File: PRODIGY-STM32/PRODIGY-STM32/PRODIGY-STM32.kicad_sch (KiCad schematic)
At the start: 4 parts

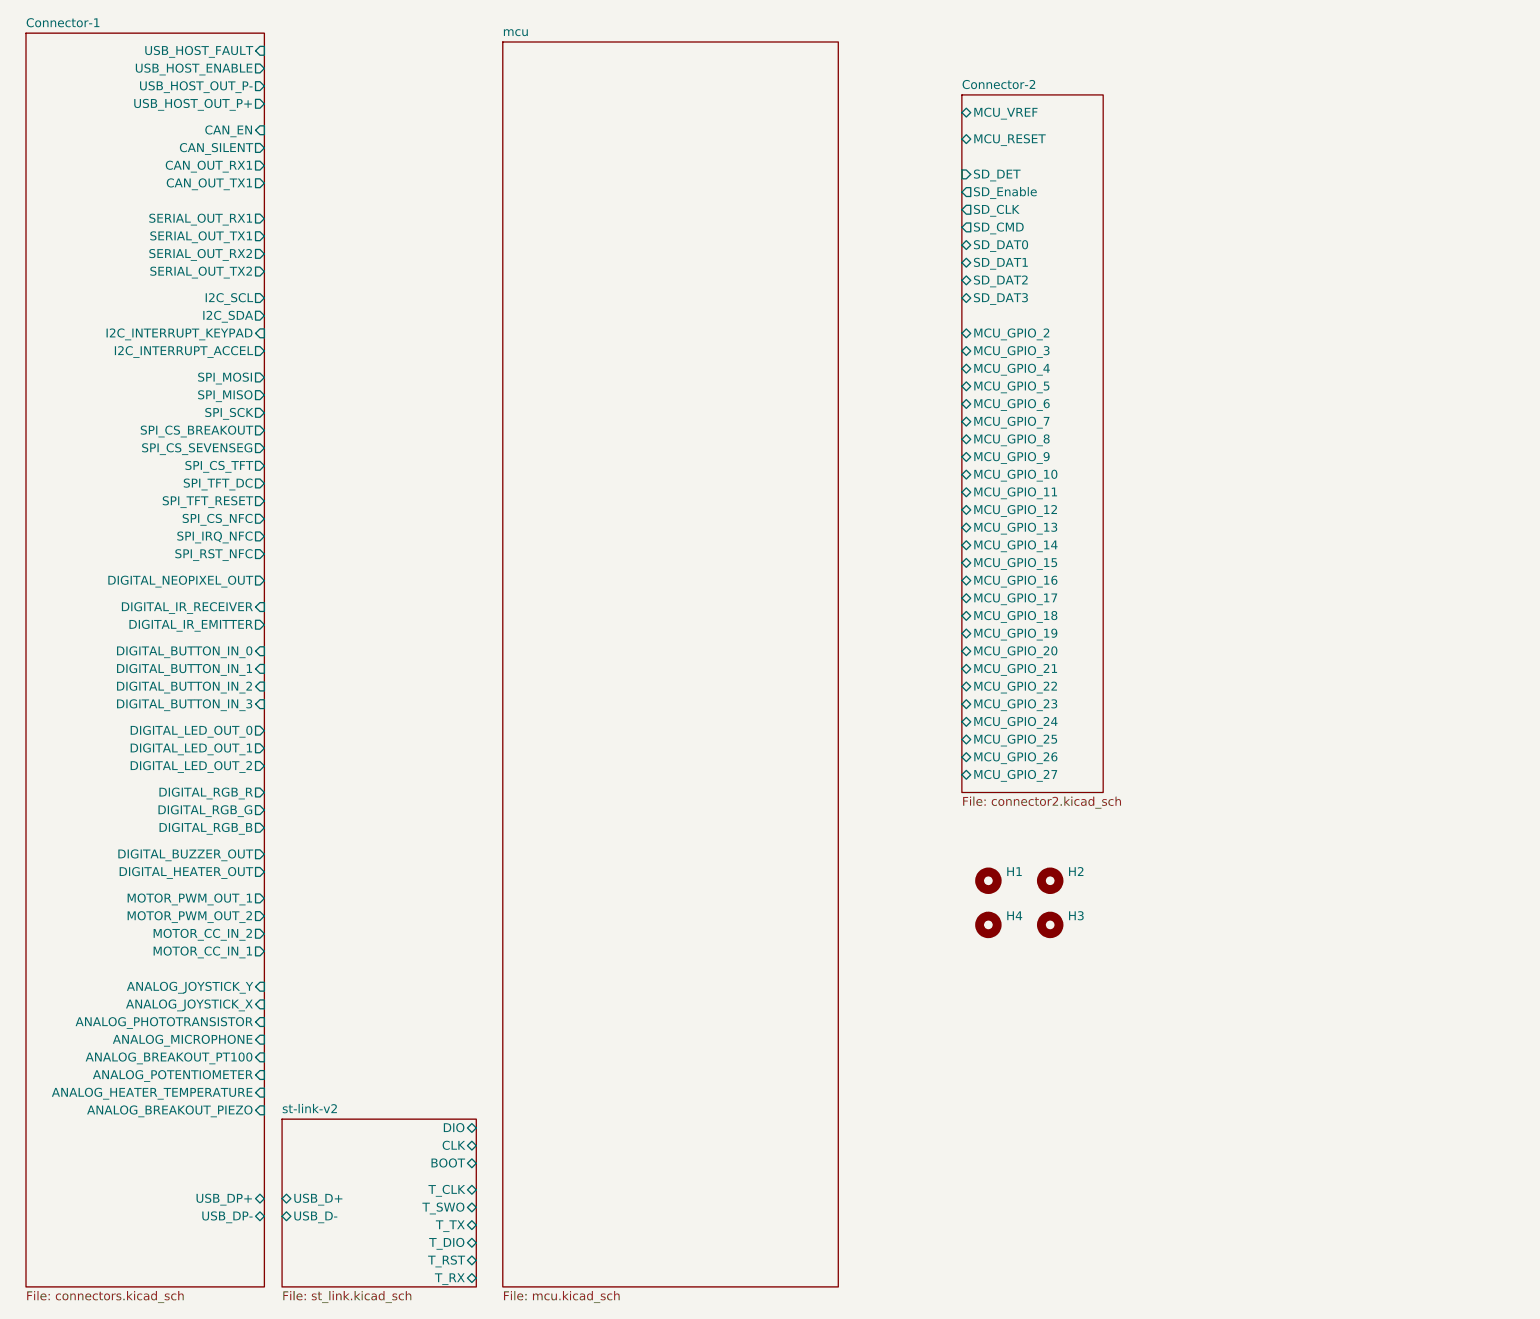
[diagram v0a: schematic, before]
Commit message: stm32 schematic finished
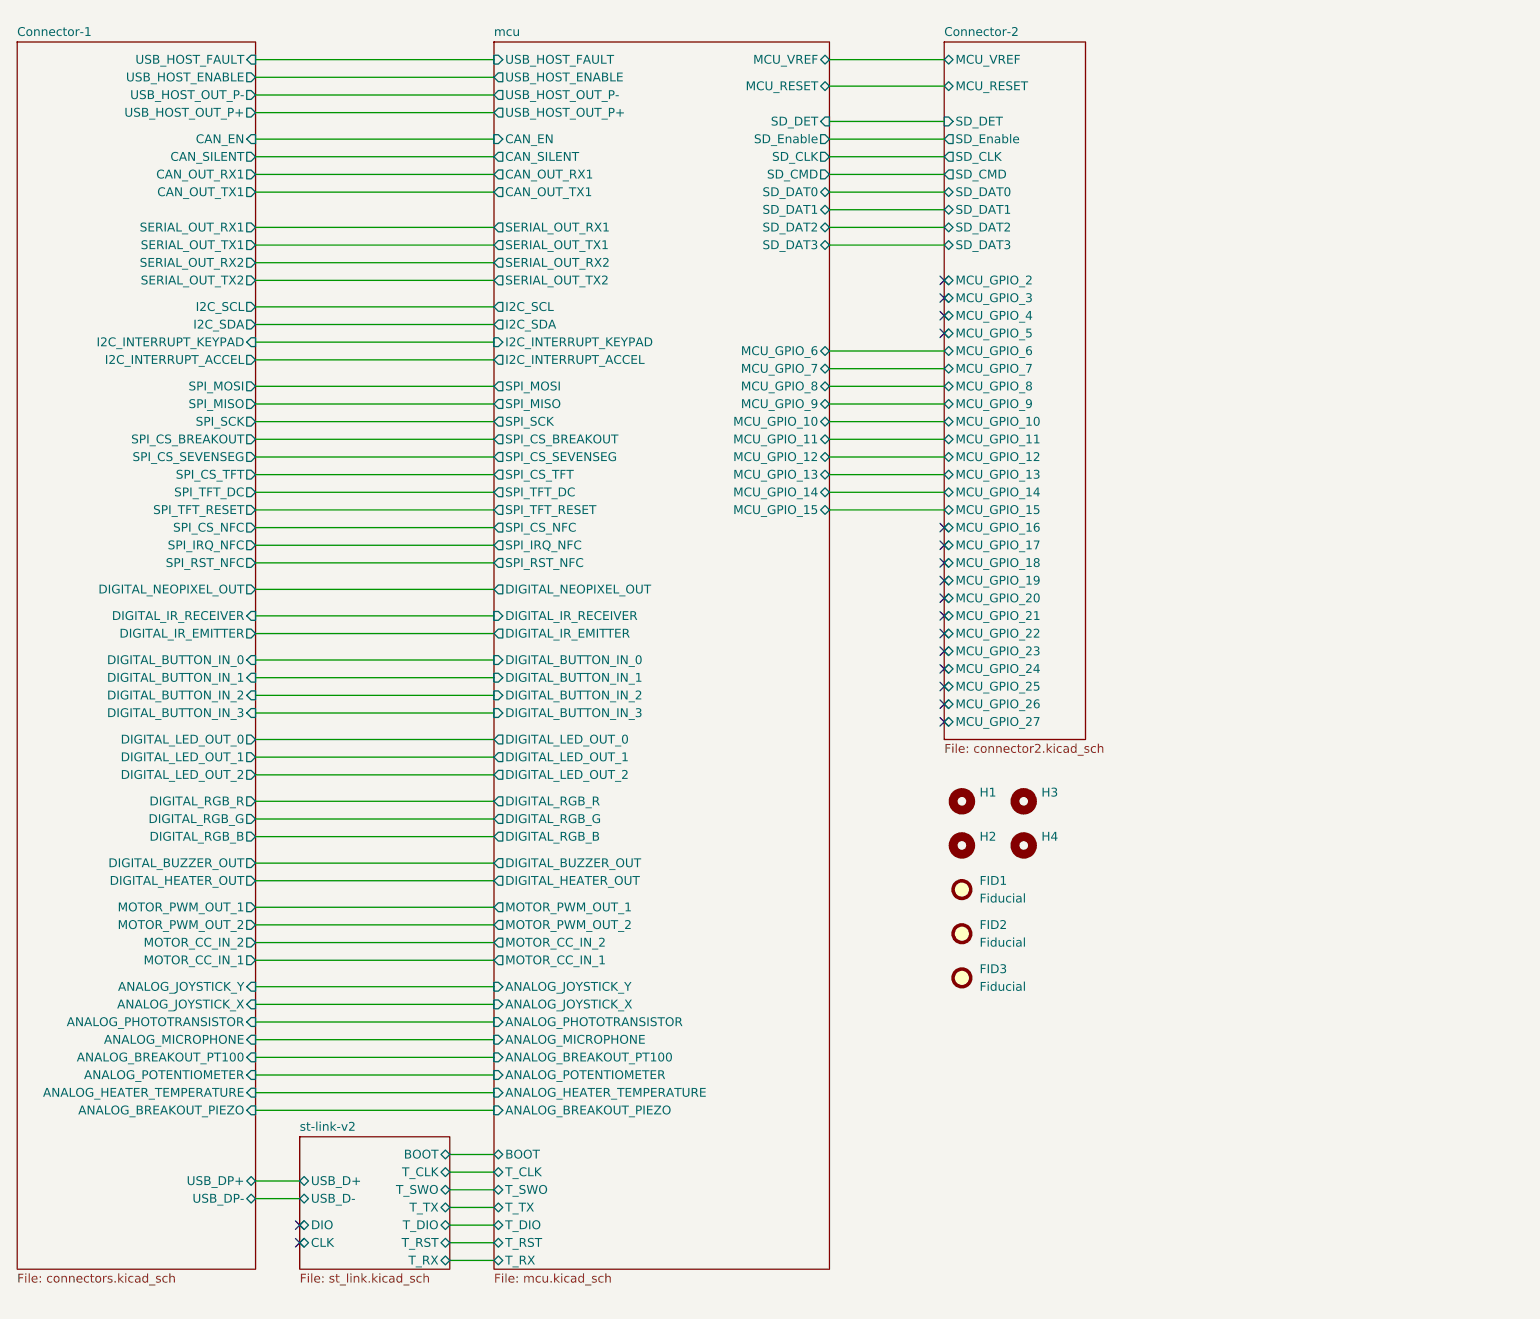
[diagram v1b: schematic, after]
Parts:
- added FID1, FID2, FID3: Fiducial, symbol Mechanical:Fiducial
- renumbered H4 to H2, H2 to H3, H3 to H4
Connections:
- no-connect marks 0 -> 18
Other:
- sheet mcu ports: added ANALOG_BREAKOUT_PIEZO, ANALOG_BREAKOUT_PT100, ANALOG_HEATER_TEMPERATURE, ANALOG_JOYSTICK_X, ANALOG_JOYSTICK_Y, ANALOG_MICROPHONE, ANALOG_PHOTOTRANSISTOR, ANALOG_POTENTIOMETER, BOOT, CAN_EN, CAN_OUT_RX1, CAN_OUT_TX1, CAN_SILENT, DIGITAL_BUTTON_IN_0, DIGITAL_BUTTON_IN_1, DIGITAL_BUTTON_IN_2, DIGITAL_BUTTON_IN_3, DIGITAL_BUZZER_OUT, DIGITAL_HEATER_OUT, DIGITAL_IR_EMITTER, DIGITAL_IR_RECEIVER, DIGITAL_LED_OUT_0, DIGITAL_LED_OUT_1, DIGITAL_LED_OUT_2, DIGITAL_NEOPIXEL_OUT, DIGITAL_RGB_B, DIGITAL_RGB_G, DIGITAL_RGB_R, I2C_INTERRUPT_ACCEL, I2C_INTERRUPT_KEYPAD, I2C_SCL, I2C_SDA, MCU_GPIO_10, MCU_GPIO_11, MCU_GPIO_12, MCU_GPIO_13, MCU_GPIO_14, MCU_GPIO_15, MCU_GPIO_6, MCU_GPIO_7, MCU_GPIO_8, MCU_GPIO_9, MCU_RESET, MCU_VREF, MOTOR_CC_IN_1, MOTOR_CC_IN_2, MOTOR_PWM_OUT_1, MOTOR_PWM_OUT_2, SD_CLK, SD_CMD, SD_DAT0, SD_DAT1, SD_DAT2, SD_DAT3, SD_DET, SD_Enable, SERIAL_OUT_RX1, SERIAL_OUT_RX2, SERIAL_OUT_TX1, SERIAL_OUT_TX2, SPI_CS_BREAKOUT, SPI_CS_NFC, SPI_CS_SEVENSEG, SPI_CS_TFT, SPI_IRQ_NFC, SPI_MISO, SPI_MOSI, SPI_RST_NFC, SPI_SCK, SPI_TFT_DC, SPI_TFT_RESET, T_CLK, T_DIO, T_RST, T_RX, T_SWO, T_TX, USB_HOST_ENABLE, USB_HOST_FAULT, USB_HOST_OUT_P+, USB_HOST_OUT_P-; removed none
- moved on the sheet: H1, H2, H3, H4

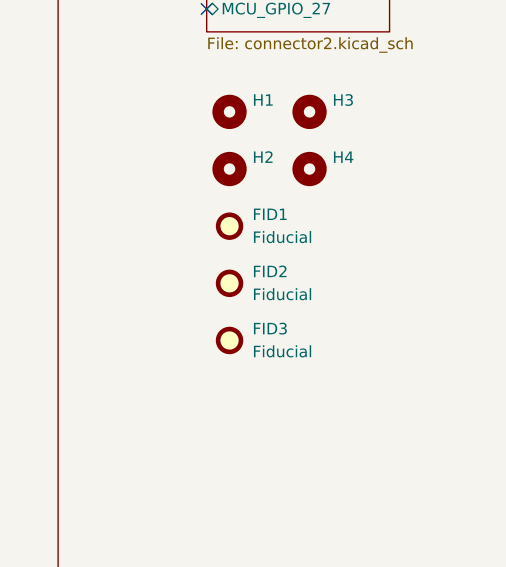
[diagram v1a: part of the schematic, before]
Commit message: All footprint assosiations have been made across all schematics.
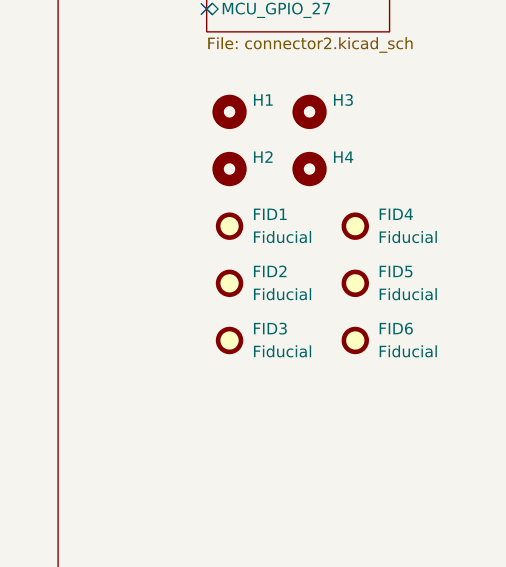
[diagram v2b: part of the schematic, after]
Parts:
- added FID4, FID5, FID6: Fiducial, Fiducial:Fiducial_1mm_Mask3mm, symbol Mechanical:Fiducial
- FID1, FID2, FID3: footprint (none) -> Fiducial:Fiducial_1mm_Mask3mm
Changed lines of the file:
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@@
 			)
 		)
-		(property "Footprint" ""
+		(property "Footprint" "Fiducial:Fiducial_1mm_Mask3mm"
 			(at 186.69 144.78 0)
 			(effects
@@
 	(symbol
 		(lib_id "Mechanical:Fiducial")
+		(at 200.66 151.13 0)
+		(unit 1)
+		(exclude_from_sim no)
+		(in_bom yes)
+		(on_board yes)
+		(dnp no)
+		(fields_autoplaced yes)
+		(property "Reference" "FID6"
+			(at 203.2 149.8599 0)
+			(effects
+				(font
+					(size 1.27 1.27)
+				)
+				(justify left)
+			)
+		)
+		(property "Value" "Fiducial"
+			(at 203.2 152.3999 0)
+			(effects
+				(font
+					(size 1.27 1.27)
+				)
+				(justify left)
+			)
+		)
+		(property "Footprint" "Fiducial:Fiducial_1mm_Mask3mm"
+			(at 200.66 151.13 0)
+			(effects
+				(font
+					(size 1.27 1.27)
+				)
+				(hide yes)
+			)
+		)
+		(property "Datasheet" "~"
+			(at 200.66 151.13 0)
+			(effects
+				(font
+					(size 1.27 1.27)
+				)
+				(hide yes)
+			)
+		)
+		(property "Description" "Fiducial Marker"
+			(at 200.66 151.13 0)
+			(effects
+				(font
+					(size 1.27 1.27)
+				)
+				(hide yes)
+			)
+		)
+		(instances
+			(project "PRODIGY-STM32"
+				(path "/f2f1c781-b8fe-416b-b7a0-b424640c1d9f"
+					(reference "FID6")
+					(unit 1)
+				)
+			)
+		)
+	)
+	(symbol
+		(lib_id "Mechanical:Fiducial")
 		(at 186.69 151.13 0)
 		(unit 1)
@@
 			)
 		)
-		(property "Footprint" ""
+		(property "Footprint" "Fiducial:Fiducial_1mm_Mask3mm"
 			(at 186.69 151.13 0)
 			(effects
@@
 	)
 	(symbol
+		(lib_id "Mechanical:Fiducial")
+		(at 200.66 138.43 0)
+		(unit 1)
+		(exclude_from_sim no)
+		(in_bom yes)
+		(on_board yes)
+		(dnp no)
+		(fields_autoplaced yes)
+		(property "Reference" "FID4"
+			(at 203.2 137.1599 0)
+			(effects
+				(font
+					(size 1.27 1.27)
+				)
+				(justify left)
+			)
+		)
+		(property "Value" "Fiducial"
+			(at 203.2 139.6999 0)
+			(effects
+				(font
+					(size 1.27 1.27)
+				)
+				(justify left)
+			)
+		)
+		(property "Footprint" "Fiducial:Fiducial_1mm_Mask3mm"
+			(at 200.66 138.43 0)
+			(effects
+				(font
+					(size 1.27 1.27)
+				)
+				(hide yes)
+			)
+		)
+		(property "Datasheet" "~"
+			(at 200.66 138.43 0)
+			(effects
+				(font
+					(size 1.27 1.27)
+				)
+				(hide yes)
+			)
+		)
+		(property "Description" "Fiducial Marker"
+			(at 200.66 138.43 0)
+			(effects
+				(font
+					(size 1.27 1.27)
+				)
+				(hide yes)
+			)
+		)
+		(instances
+			(project "PRODIGY-STM32"
+				(path "/f2f1c781-b8fe-416b-b7a0-b424640c1d9f"
+					(reference "FID4")
+					(unit 1)
+				)
+			)
+		)
+	)
+	(symbol
 		(lib_id "Mechanical:MountingHole")
 		(at 186.69 132.08 0)
@@
 	)
 	(symbol
+		(lib_id "Mechanical:Fiducial")
+		(at 200.66 144.78 0)
+		(unit 1)
+		(exclude_from_sim no)
+		(in_bom yes)
+		(on_board yes)
+		(dnp no)
+		(fields_autoplaced yes)
+		(property "Reference" "FID5"
+			(at 203.2 143.5099 0)
+			(effects
+				(font
+					(size 1.27 1.27)
+				)
+				(justify left)
+			)
+		)
+		(property "Value" "Fiducial"
+			(at 203.2 146.0499 0)
+			(effects
+				(font
+					(size 1.27 1.27)
+				)
+				(justify left)
+			)
+		)
+		(property "Footprint" "Fiducial:Fiducial_1mm_Mask3mm"
+			(at 200.66 144.78 0)
+			(effects
+				(font
+					(size 1.27 1.27)
+				)
+				(hide yes)
+			)
+		)
+		(property "Datasheet" "~"
+			(at 200.66 144.78 0)
+			(effects
+				(font
+					(size 1.27 1.27)
+				)
+				(hide yes)
+			)
+		)
+		(property "Description" "Fiducial Marker"
+			(at 200.66 144.78 0)
+			(effects
+				(font
+					(size 1.27 1.27)
+				)
+				(hide yes)
+			)
+		)
+		(instances
+			(project "PRODIGY-STM32"
+				(path "/f2f1c781-b8fe-416b-b7a0-b424640c1d9f"
+					(reference "FID5")
+					(unit 1)
+				)
+			)
+		)
+	)
+	(symbol
 		(lib_id "Mechanical:MountingHole")
 		(at 195.58 132.08 0)
@@
 			)
 		)
-		(property "Footprint" ""
+		(property "Footprint" "Fiducial:Fiducial_1mm_Mask3mm"
 			(at 186.69 138.43 0)
 			(effects

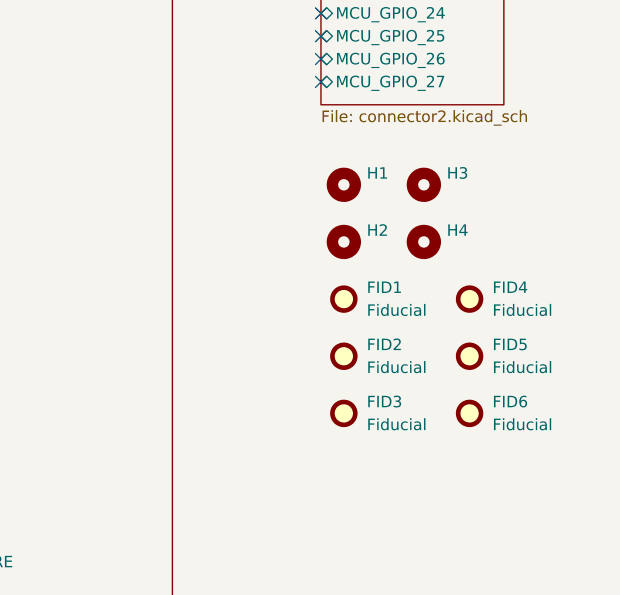
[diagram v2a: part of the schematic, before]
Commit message: STM32 bom done.
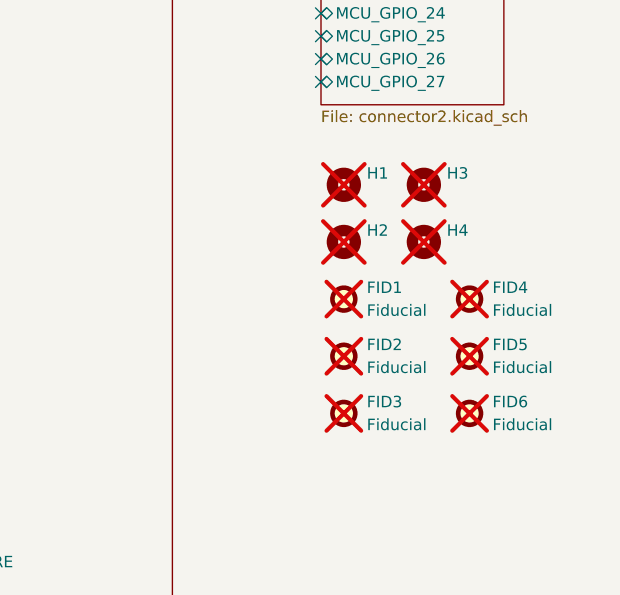
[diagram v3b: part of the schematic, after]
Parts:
- FID1, FID2, FID3, FID4, FID5, FID6, H1, H2, H3, H4: now not fitted
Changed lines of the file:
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@@
 		(in_bom yes)
 		(on_board yes)
-		(dnp no)
+		(dnp yes)
 		(fields_autoplaced yes)
 		(property "Reference" "H1"
@@
 			)
 		)
+		(property "MOUSER" ""
+			(at 186.69 125.73 0)
+			(effects
+				(font
+					(size 1.27 1.27)
+				)
+				(hide yes)
+			)
+		)
+		(property "TME" ""
+			(at 186.69 125.73 0)
+			(effects
+				(font
+					(size 1.27 1.27)
+				)
+				(hide yes)
+			)
+		)
 		(instances
 			(project ""
@@
 		(in_bom yes)
 		(on_board yes)
-		(dnp no)
+		(dnp yes)
 		(fields_autoplaced yes)
 		(property "Reference" "FID2"
@@
 			)
 		)
+		(property "MOUSER" ""
+			(at 186.69 144.78 0)
+			(effects
+				(font
+					(size 1.27 1.27)
+				)
+				(hide yes)
+			)
+		)
+		(property "TME" ""
+			(at 186.69 144.78 0)
+			(effects
+				(font
+					(size 1.27 1.27)
+				)
+				(hide yes)
+			)
+		)
 		(instances
 			(project "PRODIGY-STM32"
@@
 		(in_bom yes)
 		(on_board yes)
-		(dnp no)
+		(dnp yes)
 		(fields_autoplaced yes)
 		(property "Reference" "H3"
@@
 			)
 		)
+		(property "MOUSER" ""
+			(at 195.58 125.73 0)
+			(effects
+				(font
+					(size 1.27 1.27)
+				)
+				(hide yes)
+			)
+		)
+		(property "TME" ""
+			(at 195.58 125.73 0)
+			(effects
+				(font
+					(size 1.27 1.27)
+				)
+				(hide yes)
+			)
+		)
 		(instances
 			(project "PRODIGY-STM32"
@@
 		(in_bom yes)
 		(on_board yes)
-		(dnp no)
+		(dnp yes)
 		(fields_autoplaced yes)
 		(property "Reference" "FID6"
@@
 			)
 		)
+		(property "MOUSER" ""
+			(at 200.66 151.13 0)
+			(effects
+				(font
+					(size 1.27 1.27)
+				)
+				(hide yes)
+			)
+		)
+		(property "TME" ""
+			(at 200.66 151.13 0)
+			(effects
+				(font
+					(size 1.27 1.27)
+				)
+				(hide yes)
+			)
+		)
 		(instances
 			(project "PRODIGY-STM32"
@@
 		(in_bom yes)
 		(on_board yes)
-		(dnp no)
+		(dnp yes)
 		(fields_autoplaced yes)
 		(property "Reference" "FID3"
@@
 			)
 		)
+		(property "MOUSER" ""
+			(at 186.69 151.13 0)
+			(effects
+				(font
+					(size 1.27 1.27)
+				)
+				(hide yes)
+			)
+		)
+		(property "TME" ""
+			(at 186.69 151.13 0)
+			(effects
+				(font
+					(size 1.27 1.27)
+				)
+				(hide yes)
+			)
+		)
 		(instances
 			(project "PRODIGY-STM32"
@@
 		(in_bom yes)
 		(on_board yes)
-		(dnp no)
+		(dnp yes)
 		(fields_autoplaced yes)
 		(property "Reference" "FID4"
@@
 			)
 		)
+		(property "MOUSER" ""
+			(at 200.66 138.43 0)
+			(effects
+				(font
+					(size 1.27 1.27)
+				)
+				(hide yes)
+			)
+		)
+		(property "TME" ""
+			(at 200.66 138.43 0)
+			(effects
+				(font
+					(size 1.27 1.27)
+				)
+				(hide yes)
+			)
+		)
 		(instances
 			(project "PRODIGY-STM32"
@@
 		(in_bom yes)
 		(on_board yes)
-		(dnp no)
+		(dnp yes)
 		(fields_autoplaced yes)
 		(property "Reference" "H2"
@@
 			)
 		)
+		(property "MOUSER" ""
+			(at 186.69 132.08 0)
+			(effects
+				(font
+					(size 1.27 1.27)
+				)
+				(hide yes)
+			)
+		)
+		(property "TME" ""
+			(at 186.69 132.08 0)
+			(effects
+				(font
+					(size 1.27 1.27)
+				)
+				(hide yes)
+			)
+		)
 		(instances
 			(project "PRODIGY-STM32"
@@
 		(in_bom yes)
 		(on_board yes)
-		(dnp no)
+		(dnp yes)
 		(fields_autoplaced yes)
 		(property "Reference" "FID5"
@@
 			)
 		)
+		(property "MOUSER" ""
+			(at 200.66 144.78 0)
+			(effects
+				(font
+					(size 1.27 1.27)
+				)
+				(hide yes)
+			)
+		)
+		(property "TME" ""
+			(at 200.66 144.78 0)
+			(effects
+				(font
+					(size 1.27 1.27)
+				)
+				(hide yes)
+			)
+		)
 		(instances
 			(project "PRODIGY-STM32"
@@
 		(in_bom yes)
 		(on_board yes)
-		(dnp no)
+		(dnp yes)
 		(fields_autoplaced yes)
 		(property "Reference" "H4"
@@
 			)
 		)
+		(property "MOUSER" ""
+			(at 195.58 132.08 0)
+			(effects
+				(font
+					(size 1.27 1.27)
+				)
+				(hide yes)
+			)
+		)
+		(property "TME" ""
+			(at 195.58 132.08 0)
+			(effects
+				(font
+					(size 1.27 1.27)
+				)
+				(hide yes)
+			)
+		)
 		(instances
 			(project "PRODIGY-STM32"
@@
 		(in_bom yes)
 		(on_board yes)
-		(dnp no)
+		(dnp yes)
 		(fields_autoplaced yes)
 		(property "Reference" "FID1"
@@
 			(at 186.69 138.43 0)
 			(effects
+				(font
+					(size 1.27 1.27)
+				)
+				(hide yes)
+			)
+		)
+		(property "MOUSER" ""
+			(at 186.69 138.43 0)
+			(effects
+				(font
+					(size 1.27 1.27)
+				)
+				(hide yes)
+			)
+		)
+		(property "TME" ""
+			(at 186.69 138.43 0)
+			(effects
